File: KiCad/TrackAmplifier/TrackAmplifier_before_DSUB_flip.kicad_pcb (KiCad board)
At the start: 2 copper layers, 105 x 70 mm, 108 parts, among them J1 DB15_Male_MountingHoles, J2 Conn_01x06, Q1 2N7002, U1 ST485EBDR, U10 REF3025, U11 LM35-LP, U2 ST485EBDR, U3 LM78M05_TO252, U4 LMD18200, U5 ST485EBDR, U6 ST485EBDR, U7 INA326, U8 INA326, U9 PIC16F18854-SO

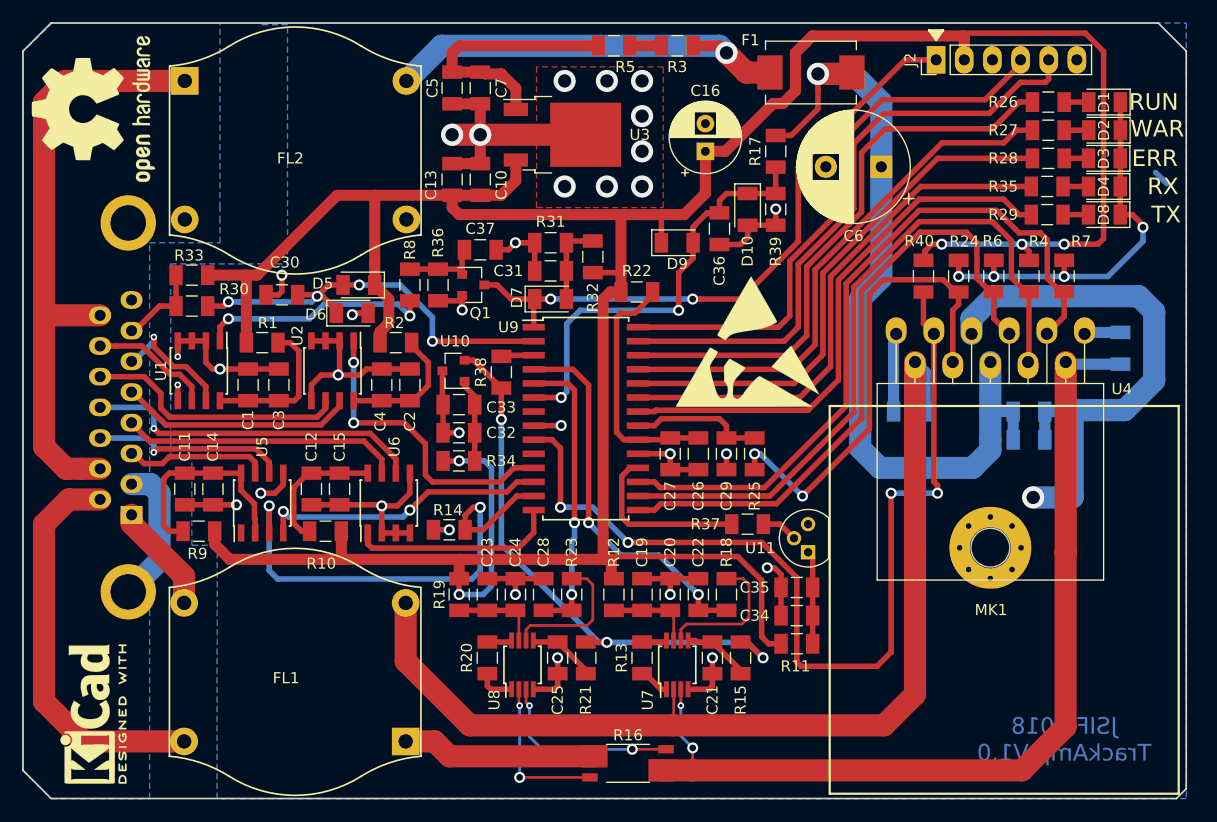
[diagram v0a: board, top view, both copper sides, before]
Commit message: Updated chematic and pcb according to fit test
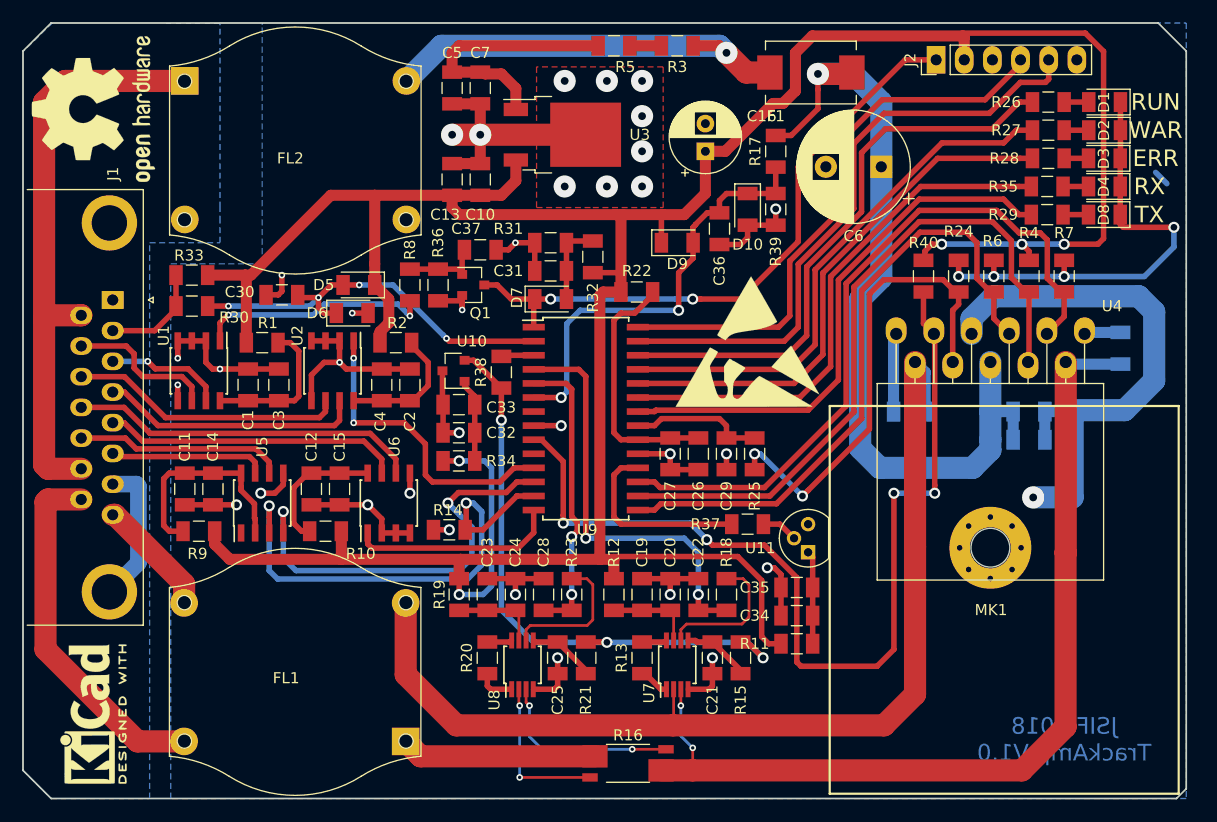
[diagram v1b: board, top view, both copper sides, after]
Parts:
- J1: moved to F.Cu
- moved J1 19.5 mm to (58.1, 75.0), turned to 270 degrees
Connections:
- J1 pad 1: PWMO2 -> GNDD
- J1 pad 10: Net-(FL2-Pad1) -> Reset_A
- J1 pad 11: TX_A -> Sync_A
- J1 pad 13: Sync_A -> TX_A
- J1 pad 14: Reset_A -> Net-(FL2-Pad1)
- J1 pad 15: Net-(FL2-Pad1) -> PWMO1
- J1 pad 2: GNDD -> ID_R
- J1 pad 3: TX_B -> Reset_B
- J1 pad 4: RX_B -> Sync_B
- J1 pad 5: Sync_B -> RX_B
- J1 pad 6: Reset_B -> TX_B
- J1 pad 7: ID_R -> GNDD
- J1 pad 8: GNDD -> PWMO2
- J1 pad 9: PWMO1 -> Net-(FL2-Pad1)
- MK1 pad 1: (no net) -> GND
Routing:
- net TX: track 26.3 -> 38.7 mm
- net PWMO1: track 36.1 -> 32.6 mm
- net BMF: track 34.5 -> 38.0 mm
- net VREF: track 50.9 -> 54.3 mm
- net Sync_B: track 20.7 -> 23.2 mm
- net GND: track 235.4 -> 237.9 mm, vias 37 -> 38
- net Reset_A: track 11.1 -> 13.5 mm
- net Net-(FL2-Pad1): track 55.7 -> 53.3 mm
- net ID_R: track 7.72 -> 9.59 mm
- net RX_B: track 25.2 -> 26.9 mm
- net TEMP: track 15.7 -> 17.1 mm
- net TX_B: track 13.0 -> 14.2 mm
- net Sync_A: track 23.4 -> 24.5 mm
- net TX_A: track 17.8 -> 18.9 mm, vias 1 -> 0
- net ID: track 37.9 -> 37.0 mm
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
